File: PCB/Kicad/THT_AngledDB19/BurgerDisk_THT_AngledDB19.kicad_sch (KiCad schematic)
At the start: 15 parts, among them J1 Daisy port in, J2 MicroSD module, J3 UART, J4 Daisy port out, U1 PC817

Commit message: Add tooling to create JLCPCB BOM/CPL files
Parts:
- J2: footprint Connector_PinHeader_2.54mm:PinHeader_1x06_P2.54mm_Horizontal -> Connector_PinHeader_2.54mm:PinHeader_1x06_P2.54mm_Vertical
- R3: LCSC C61239 -> C129899
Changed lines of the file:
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@@
       (effects (font (size 1.27 1.27)))
     )
-    (property "Footprint" "Connector_PinHeader_2.54mm:PinHeader_1x06_P2.54mm_Horizontal" (at 99.06 132.08 0)
+    (property "Footprint" "Connector_PinHeader_2.54mm:PinHeader_1x06_P2.54mm_Vertical" (at 99.06 132.08 0)
       (effects (font (size 1.27 1.27)) hide)
     )
@@
       (effects (font (size 1.27 1.27)) hide)
     )
-    (property "LCSC" "C61239" (at 99.06 68.58 0)
+    (property "LCSC" "C129899" (at 99.06 68.58 0)
       (effects (font (size 1.27 1.27)) hide)
     )

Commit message: Small esthetic fixes
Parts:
- J1: LCSC C17463886 -> C305958
- J2: footprint Connector_PinHeader_2.54mm:PinHeader_1x06_P2.54mm_Vertical -> Connector_PinHeader_2.54mm:PinHeader_1x06_P2.54mm_Horizontal
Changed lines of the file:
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@@
       (effects (font (size 1.27 1.27)))
     )
-    (property "Footprint" "Connector_PinHeader_2.54mm:PinHeader_1x06_P2.54mm_Vertical" (at 99.06 132.08 0)
+    (property "Footprint" "Connector_PinHeader_2.54mm:PinHeader_1x06_P2.54mm_Horizontal" (at 99.06 132.08 0)
       (effects (font (size 1.27 1.27)) hide)
     )
@@
       (effects (font (size 1.27 1.27)) hide)
     )
-    (property "LCSC" "C17463886" (at 129.54 36.83 0)
+    (property "LCSC" "C305958" (at 129.54 36.83 0)
       (effects (font (size 1.27 1.27)) hide)
     )

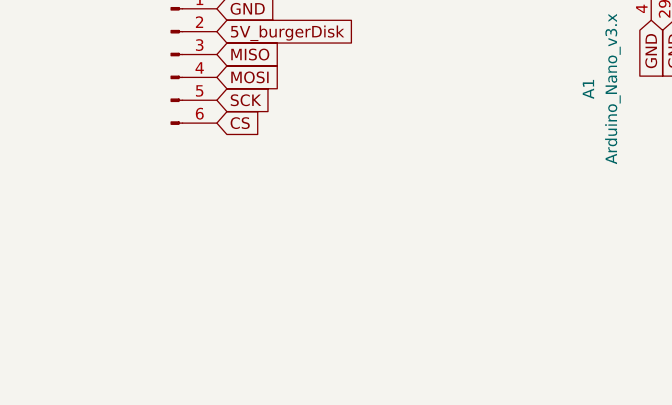
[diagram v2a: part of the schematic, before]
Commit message: Add 8-pin header for full size SD module
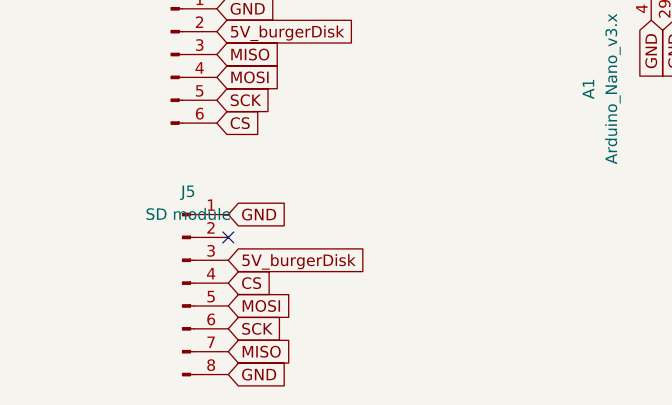
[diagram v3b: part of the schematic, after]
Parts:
- added J5: SD module, Connector_PinHeader_2.54mm:PinHeader_1x08_P2.54mm_Vertical, symbol Connector:Conn_01x08_Pin
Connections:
- net 5V_burgerDisk: now also J5.3 (Pin_3)
- net CS: now also J5.4 (Pin_4)
- net GND: now also J5.1 (Pin_1), J5.8 (Pin_8)
- net MISO: now also J5.7 (Pin_7)
- net MOSI: now also J5.5 (Pin_5)
- net SCK: now also J5.6 (Pin_6)
- no-connect marks 9 -> 10
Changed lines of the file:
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@@
   (no_connect (at 154.94 77.47))
   (no_connect (at 165.1 120.65))
+  (no_connect (at 105.41 152.4))
   (no_connect (at 165.1 87.63))
   (no_connect (at 165.1 97.79))
@@
     )
   )
+  (global_label "CS" (shape input) (at 105.41 157.48 0) (fields_autoplaced)
+    (effects (font (size 1.27 1.27)) (justify left))
+    (property "Intersheetrefs" "${INTERSHEET_REFS}" (at 110.8747 157.48 0)
+      (effects (font (size 1.27 1.27)) (justify left) hide)
+    )
+  )
   (global_label "PH1" (shape input) (at 139.7 95.25 180) (fields_autoplaced)
     (effects (font (size 1.27 1.27)) (justify right))
@@
     )
   )
+  (global_label "SCK" (shape input) (at 105.41 162.56 0) (fields_autoplaced)
+    (effects (font (size 1.27 1.27)) (justify left))
+    (property "Intersheetrefs" "${INTERSHEET_REFS}" (at 112.1447 162.56 0)
+      (effects (font (size 1.27 1.27)) (justify left) hide)
+    )
+  )
   (global_label "RDDATA_in" (shape input) (at 139.7 102.87 180) (fields_autoplaced)
     (effects (font (size 1.27 1.27)) (justify right))
@@
     )
   )
+  (global_label "MISO" (shape input) (at 105.41 165.1 0) (fields_autoplaced)
+    (effects (font (size 1.27 1.27)) (justify left))
+    (property "Intersheetrefs" "${INTERSHEET_REFS}" (at 112.9914 165.1 0)
+      (effects (font (size 1.27 1.27)) (justify left) hide)
+    )
+  )
   (global_label "DRV2_burgerDisk" (shape input) (at 139.7 110.49 180) (fields_autoplaced)
     (effects (font (size 1.27 1.27)) (justify right))
@@
     )
   )
+  (global_label "MOSI" (shape input) (at 105.41 160.02 0) (fields_autoplaced)
+    (effects (font (size 1.27 1.27)) (justify left))
+    (property "Intersheetrefs" "${INTERSHEET_REFS}" (at 112.9914 160.02 0)
+      (effects (font (size 1.27 1.27)) (justify left) hide)
+    )
+  )
   (global_label "PH2" (shape input) (at 228.6 99.06 180) (fields_autoplaced)
     (effects (font (size 1.27 1.27)) (justify right))
@@
     )
   )
+  (global_label "GND" (shape input) (at 105.41 167.64 0) (fields_autoplaced)
+    (effects (font (size 1.27 1.27)) (justify left))
+    (property "Intersheetrefs" "${INTERSHEET_REFS}" (at 112.2657 167.64 0)
+      (effects (font (size 1.27 1.27)) (justify left) hide)
+    )
+  )
   (global_label "PH3_out" (shape input) (at 228.6 104.14 180) (fields_autoplaced)
     (effects (font (size 1.27 1.27)) (justify right))
@@
     )
   )
+  (global_label "5V_burgerDisk" (shape input) (at 105.41 154.94 0) (fields_autoplaced)
+    (effects (font (size 1.27 1.27)) (justify left))
+    (property "Intersheetrefs" "${INTERSHEET_REFS}" (at 121.6999 154.94 0)
+      (effects (font (size 1.27 1.27)) (justify left) hide)
+    )
+  )
   (global_label "GND" (shape input) (at 93.98 72.39 90) (fields_autoplaced)
     (effects (font (size 1.27 1.27)) (justify left))
@@
     (effects (font (size 1.27 1.27)) (justify left))
     (property "Intersheetrefs" "${INTERSHEET_REFS}" (at 145.3461 36.83 0)
+      (effects (font (size 1.27 1.27)) (justify left) hide)
+    )
+  )
+  (global_label "GND" (shape input) (at 105.41 149.86 0) (fields_autoplaced)
+    (effects (font (size 1.27 1.27)) (justify left))
+    (property "Intersheetrefs" "${INTERSHEET_REFS}" (at 112.2657 149.86 0)
       (effects (font (size 1.27 1.27)) (justify left) hide)
     )
@@
         )
       )
+    )
+  )
+  (symbol (lib_id "Connector:Conn_01x08_Pin") (at 100.33 157.48 0) (unit 1)
+    (in_bom yes) (on_board yes) (dnp no)
+    (property "Reference" "J5" (at 100.965 147.32 0)
+      (effects (font (size 1.27 1.27)))
+    )
+    (property "Value" "SD module" (at 100.965 149.86 0)
+      (effects (font (size 1.27 1.27)))
+    )
+    (property "Footprint" "Connector_PinHeader_2.54mm:PinHeader_1x08_P2.54mm_Vertical" (at 100.33 157.48 0)
+      (effects (font (size 1.27 1.27)) hide)
+    )
+    (property "Datasheet" "~" (at 100.33 157.48 0)
+      (effects (font (size 1.27 1.27)) hide)
+    )
+    (property "LCSC" "C6209271" (at 100.33 157.48 0)
+      (effects (font (size 1.27 1.27)) hide)
+    )
+    (pin "4")
+    (pin "5")
+    (pin "3")
+    (pin "6")
+    (pin "1")
+    (pin "2")
+    (pin "7")
+    (pin "8")
+    (instances
+      (project "BurgerDisk_THT_AngledDB19"
+        (path "/596d0583-1d97-453e-b84c-75eed809afa2"
+          (reference "J5") (unit 1)
+        )
+      )

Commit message: Vertical footprints
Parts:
- J2: footprint Connector_PinHeader_2.54mm:PinHeader_1x06_P2.54mm_Horizontal -> Connector_PinHeader_2.54mm:PinHeader_1x06_P2.54mm_Vertical
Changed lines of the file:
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@@
       (effects (font (size 1.27 1.27)))
     )
-    (property "Footprint" "Connector_PinHeader_2.54mm:PinHeader_1x06_P2.54mm_Horizontal" (at 99.06 132.08 0)
+    (property "Footprint" "Connector_PinHeader_2.54mm:PinHeader_1x06_P2.54mm_Vertical" (at 99.06 132.08 0)
       (effects (font (size 1.27 1.27)) hide)
     )

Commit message: Add a very hacky way to add Nano headers
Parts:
- J5: LCSC C6209271 -> C124381
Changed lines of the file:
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@@
       (effects (font (size 1.27 1.27)) hide)
     )
-    (property "LCSC" "C6209271" (at 100.33 157.48 0)
+    (property "LCSC" "C124381" (at 100.33 157.48 0)
       (effects (font (size 1.27 1.27)) hide)
     )

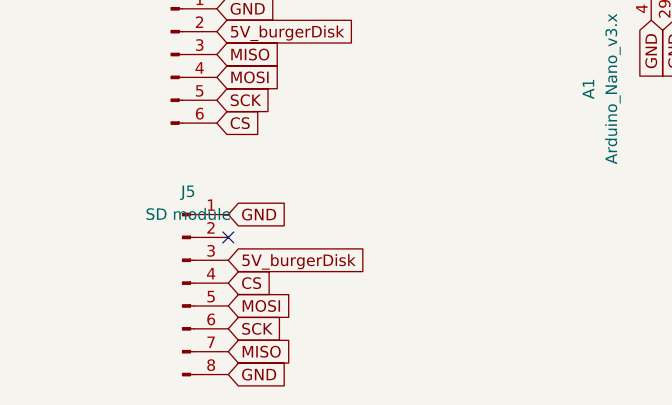
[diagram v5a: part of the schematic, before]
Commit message: Revert full-size SD connector and module.
They don't have level shifter.
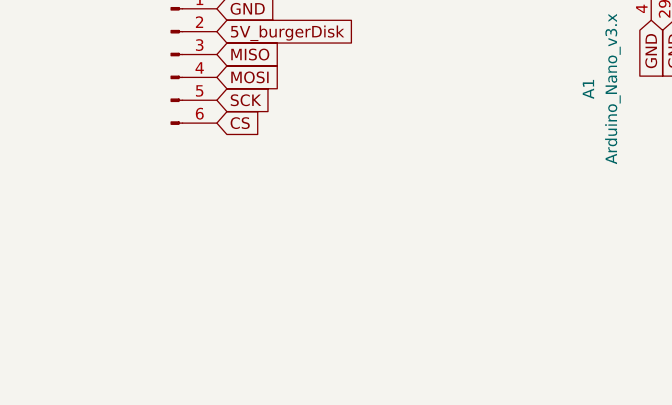
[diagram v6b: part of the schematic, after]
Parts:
- removed J5: SD module, Connector_PinHeader_2.54mm:PinHeader_1x08_P2.54mm_Vertical, symbol Connector:Conn_01x08_Pin
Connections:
- no-connect marks 10 -> 9
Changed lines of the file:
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@@
   (no_connect (at 154.94 77.47))
   (no_connect (at 165.1 120.65))
-  (no_connect (at 105.41 152.4))
   (no_connect (at 165.1 87.63))
   (no_connect (at 165.1 97.79))
@@
     )
   )
-  (global_label "CS" (shape input) (at 105.41 157.48 0) (fields_autoplaced)
-    (effects (font (size 1.27 1.27)) (justify left))
-    (property "Intersheetrefs" "${INTERSHEET_REFS}" (at 110.8747 157.48 0)
-      (effects (font (size 1.27 1.27)) (justify left) hide)
-    )
-  )
   (global_label "PH1" (shape input) (at 139.7 95.25 180) (fields_autoplaced)
     (effects (font (size 1.27 1.27)) (justify right))
@@
     )
   )
-  (global_label "SCK" (shape input) (at 105.41 162.56 0) (fields_autoplaced)
-    (effects (font (size 1.27 1.27)) (justify left))
-    (property "Intersheetrefs" "${INTERSHEET_REFS}" (at 112.1447 162.56 0)
-      (effects (font (size 1.27 1.27)) (justify left) hide)
-    )
-  )
   (global_label "RDDATA_in" (shape input) (at 139.7 102.87 180) (fields_autoplaced)
     (effects (font (size 1.27 1.27)) (justify right))
@@
     )
   )
-  (global_label "MISO" (shape input) (at 105.41 165.1 0) (fields_autoplaced)
-    (effects (font (size 1.27 1.27)) (justify left))
-    (property "Intersheetrefs" "${INTERSHEET_REFS}" (at 112.9914 165.1 0)
-      (effects (font (size 1.27 1.27)) (justify left) hide)
-    )
-  )
   (global_label "DRV2_burgerDisk" (shape input) (at 139.7 110.49 180) (fields_autoplaced)
     (effects (font (size 1.27 1.27)) (justify right))
@@
     )
   )
-  (global_label "MOSI" (shape input) (at 105.41 160.02 0) (fields_autoplaced)
-    (effects (font (size 1.27 1.27)) (justify left))
-    (property "Intersheetrefs" "${INTERSHEET_REFS}" (at 112.9914 160.02 0)
-      (effects (font (size 1.27 1.27)) (justify left) hide)
-    )
-  )
   (global_label "PH2" (shape input) (at 228.6 99.06 180) (fields_autoplaced)
     (effects (font (size 1.27 1.27)) (justify right))
@@
     )
   )
-  (global_label "GND" (shape input) (at 105.41 167.64 0) (fields_autoplaced)
-    (effects (font (size 1.27 1.27)) (justify left))
-    (property "Intersheetrefs" "${INTERSHEET_REFS}" (at 112.2657 167.64 0)
-      (effects (font (size 1.27 1.27)) (justify left) hide)
-    )
-  )
   (global_label "PH3_out" (shape input) (at 228.6 104.14 180) (fields_autoplaced)
     (effects (font (size 1.27 1.27)) (justify right))
@@
     )
   )
-  (global_label "5V_burgerDisk" (shape input) (at 105.41 154.94 0) (fields_autoplaced)
-    (effects (font (size 1.27 1.27)) (justify left))
-    (property "Intersheetrefs" "${INTERSHEET_REFS}" (at 121.6999 154.94 0)
-      (effects (font (size 1.27 1.27)) (justify left) hide)
-    )
-  )
   (global_label "GND" (shape input) (at 93.98 72.39 90) (fields_autoplaced)
     (effects (font (size 1.27 1.27)) (justify left))
@@
     (effects (font (size 1.27 1.27)) (justify left))
     (property "Intersheetrefs" "${INTERSHEET_REFS}" (at 145.3461 36.83 0)
-      (effects (font (size 1.27 1.27)) (justify left) hide)
-    )
-  )
-  (global_label "GND" (shape input) (at 105.41 149.86 0) (fields_autoplaced)
-    (effects (font (size 1.27 1.27)) (justify left))
-    (property "Intersheetrefs" "${INTERSHEET_REFS}" (at 112.2657 149.86 0)
       (effects (font (size 1.27 1.27)) (justify left) hide)
     )
@@
         )
       )
-    )
-  )
-  (symbol (lib_id "Connector:Conn_01x08_Pin") (at 100.33 157.48 0) (unit 1)
-    (in_bom yes) (on_board yes) (dnp no)
-    (property "Reference" "J5" (at 100.965 147.32 0)
-      (effects (font (size 1.27 1.27)))
-    )
-    (property "Value" "SD module" (at 100.965 149.86 0)
-      (effects (font (size 1.27 1.27)))
-    )
-    (property "Footprint" "Connector_PinHeader_2.54mm:PinHeader_1x08_P2.54mm_Vertical" (at 100.33 157.48 0)
-      (effects (font (size 1.27 1.27)) hide)
-    )
-    (property "Datasheet" "~" (at 100.33 157.48 0)
-      (effects (font (size 1.27 1.27)) hide)
-    )
-    (property "LCSC" "C124381" (at 100.33 157.48 0)
-      (effects (font (size 1.27 1.27)) hide)
-    )
-    (pin "4")
-    (pin "5")
-    (pin "3")
-    (pin "6")
-    (pin "1")
-    (pin "2")
-    (pin "7")
-    (pin "8")
-    (instances
-      (project "BurgerDisk_THT_AngledDB19"
-        (path "/596d0583-1d97-453e-b84c-75eed809afa2"
-          (reference "J5") (unit 1)
-        )
-      )

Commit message: Align connectors
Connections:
- net GND: now also J4.0
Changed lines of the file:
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@@
+    )
+  )
+  (global_label "GND" (shape input) (at 242.57 88.9 0) (fields_autoplaced)
+    (effects (font (size 1.27 1.27)) (justify left))
+    (property "Intersheetrefs" "${INTERSHEET_REFS}" (at 249.4257 88.9 0)
+      (effects (font (size 1.27 1.27)) (justify left) hide)
     )
   )
@@
     (pin "10")
     (pin "11")
+    (pin "0")
     (instances
       (project "BurgerDisk_THT_AngledDB19"
